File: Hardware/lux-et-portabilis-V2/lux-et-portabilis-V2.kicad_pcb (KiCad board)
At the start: 2 copper layers, 63 x 43 mm, 45 parts, among them J1 Conn_01x03_Socket, J2 Conn_01x03_Socket, J3 Conn_01x04_Socket, Q1 2N7002K, Q2 2N7002K, Q3 PMOS, U1 ESP32-C3-Supermini, U2 TP4056

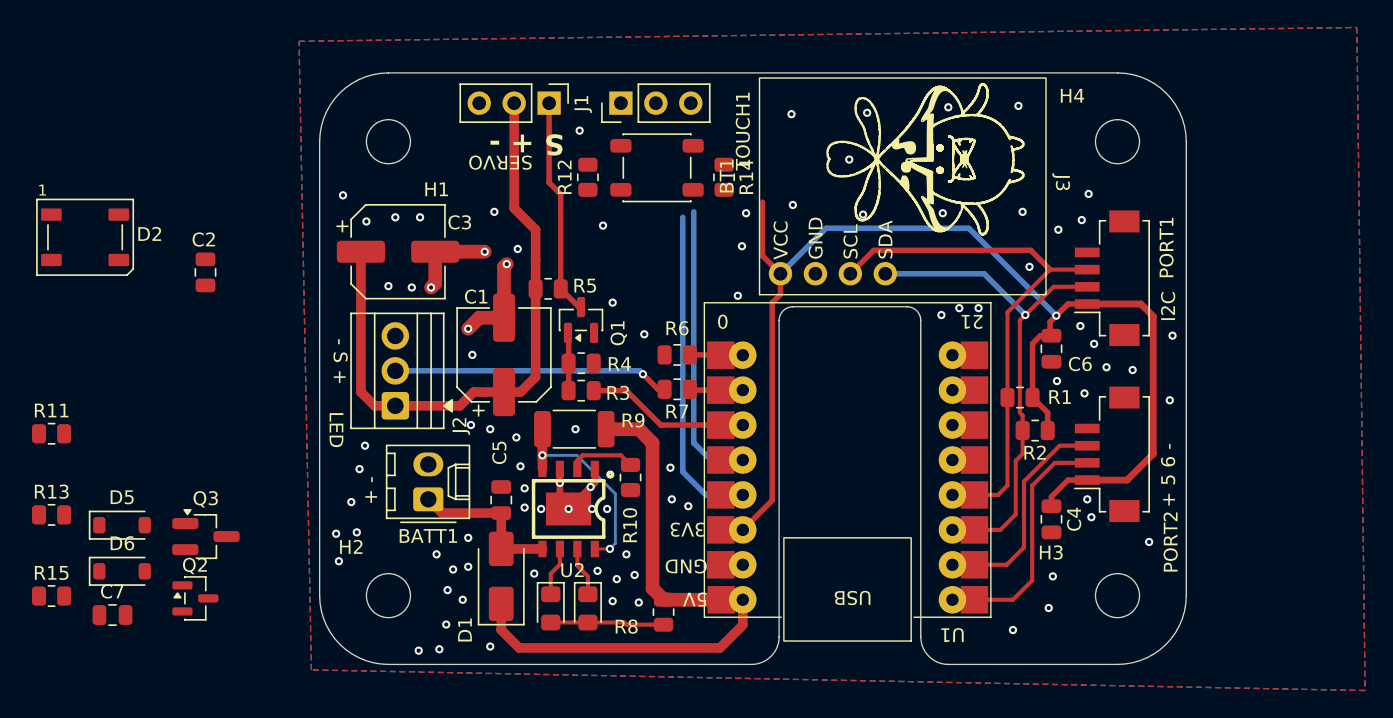
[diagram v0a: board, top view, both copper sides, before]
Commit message: Boot switch added, with connector for touch sensor
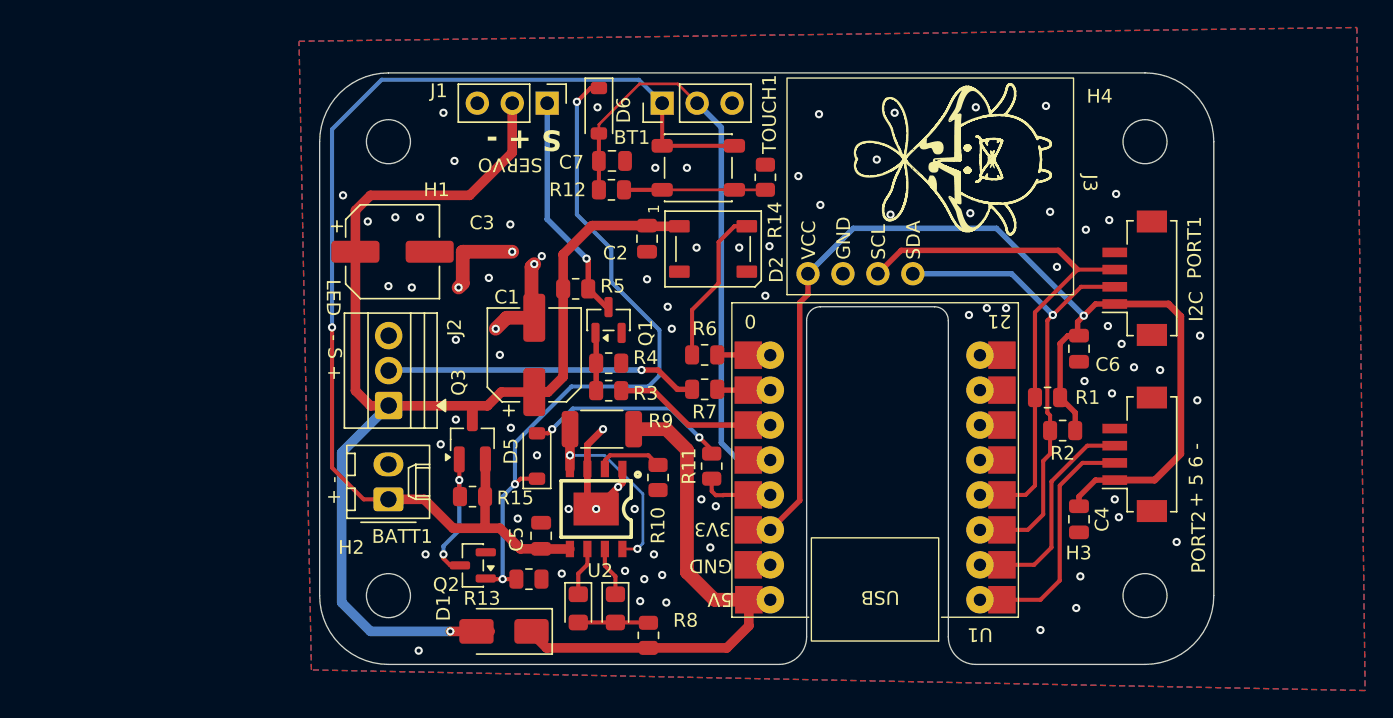
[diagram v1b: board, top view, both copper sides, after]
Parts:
- moved C7 49.1 mm to (130.8, 81.5), turned to 180 degrees
- moved D6 48.2 mm to (129.8, 77.8), turned to -90 degrees
- moved R11 48.0 mm to (138.0, 103.7), turned to 90 degrees
- moved D2 45.7 mm to (138.1, 87.9)
- moved R13 35.0 mm to (124.7, 111.9)
- moved C2 32.2 mm to (133.3, 87.2)
- moved R15 31.4 mm to (120.6, 105.9)
- moved D5 30.6 mm to (125.3, 103.0), turned to 90 degrees
- moved Q3 20.6 mm to (120.6, 101.7), turned to 90 degrees
- moved Q2 20.3 mm to (120.6, 110.9), turned to 180 degrees
- moved D1 4.00 mm to (122.9, 115.7), turned to 180 degrees
- moved C5 3.89 mm to (125.6, 108.8)
- moved BT1 3.00 mm to (137.0, 82.0)
- moved R14 3.00 mm to (141.9, 82.7)
- moved TOUCH1 3.00 mm to (134.4, 77.3)
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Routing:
- net +BATT: track 11.3 -> 83.8 mm, vias 0 -> 1
- net Net-(D5-K): track 0.00 -> 51.2 mm, vias 0 -> 3
- net V_REG: track 44.7 -> 91.9 mm, vias 0 -> 1
- net Button_GPIO: track 20.9 -> 43.2 mm
- net latch_enable: track 23.6 -> 3.69 mm
- net Net-(D5-A): track 0.00 -> 15.0 mm, vias 0 -> 2
- net Net-(D2-DIN): track 0.00 -> 11.5 mm
- net Net-(Q2-D): track 0.00 -> 10.3 mm, vias 0 -> 2
- net Net-(BT1-Pad2): track 0.00 -> 10.3 mm
- net +3.3V: track 86.7 -> 81.0 mm
- net +5V: track 42.2 -> 37.6 mm
- net GND: track 20.1 -> 23.5 mm, vias 89 -> 80
- net Net-(D3-A): track 8.27 -> 5.11 mm
- net Net-(J2-Pin_2): track 20.1 -> 22.2 mm
- net Net-(J1-Pin_1): track 15.9 -> 16.8 mm, vias 0 -> 1
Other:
- board size 63 x 43 mm -> 65 x 43 mm

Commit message: Fabrication files for Lux et Portabilis V2
Added power saving by shutting down the battery
Added onboard boot button
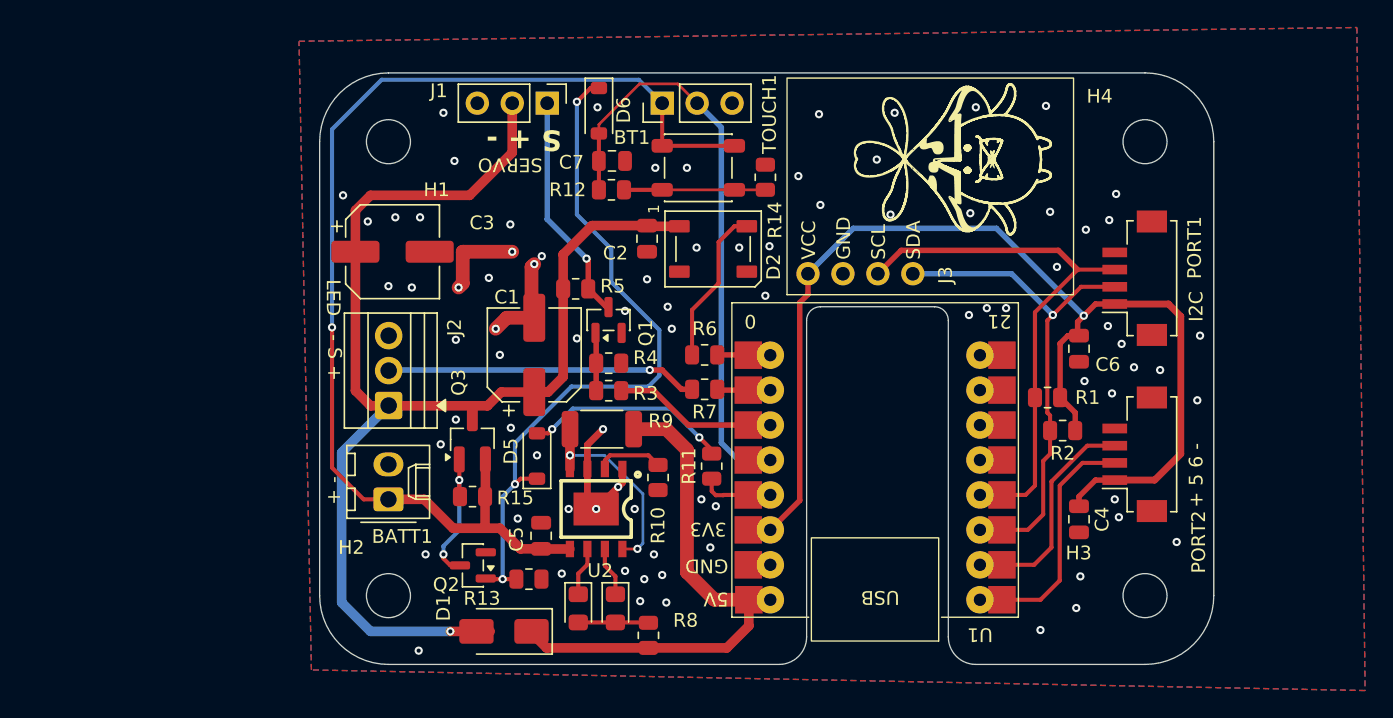
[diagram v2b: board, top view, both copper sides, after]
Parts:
- J3: footprint Custom_Footprints:MPU6050 -> Aleoexpress:MPU6050
- R1, R12, R2: value 2k2 -> 2.2k
- U1: footprint Custom_Footprints:ESP32-C3-Supermini -> Aleoexpress:ESP32-C3-Supermini
- U2: footprint Custom_Footprints:ESOP-8_L4.9-W3.9-P1.27-LS6.0-BL-EP -> Aleoexpress:ESOP-8_L4.9-W3.9-P1.27-LS6.0-BL-EP
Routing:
- net GND: vias 80 -> 82
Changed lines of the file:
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@@
 			)
 		)
-		(property "LCSC" "C77075"
+		(property "LCSC" "C15850"
 			(at 0 0 270)
 			(unlocked yes)
@@
 			)
 		)
-		(property "LCSC" "1"
+		(property "LCSC" "C7433470"
 			(at 0 0 90)
 			(unlocked yes)
@@
 		)
 	)
-	(footprint "Custom_Footprints:ESOP-8_L4.9-W3.9-P1.27-LS6.0-BL-EP"
+	(footprint "Aleoexpress:ESOP-8_L4.9-W3.9-P1.27-LS6.0-BL-EP"
 		(layer "F.Cu")
 		(at 129.6 106.8 180)
 		(property "Reference" "U2"
-			(at -0.28825 -4.4835 0)
+			(at -0.28825 -4.4835 180)
 			(layer "F.SilkS")
 			(effects
@@
 		)
 		(property "Value" "TP4056"
-			(at -0.28825 4.4835 0)
+			(at -0.28825 4.4835 180)
 			(layer "F.Fab")
 			(effects
@@
 		)
 		(property "Datasheet" "https://lcsc.com/datasheet/lcsc_datasheet_2410121619_TOPPOWER-Nanjing-Extension-Microelectronics-TP4056-42-ESOP8_C16581.pdf"
-			(at 0 0 0)
+			(at 0 0 180)
 			(layer "F.Fab")
 			(hide yes)
@@
 		)
 		(property "Description" "The Chip Type:Linear charging chip Supply Voltage:4V~6V Supply Voltage:4V~6V Maximum Charge Current:1A Charging Saturation Voltage:4.2V Type of Battery:Lithium-ion/Polymer Number of Cells:1 Number of Cells:1 Operating Temperature:-40°C~+85°C Operating Tempe"
-			(at 0 0 0)
-			(layer "F.Fab")
-			(hide yes)
-			(effects
-				(font
-					(size 1 1)
-					(thickness 0.15)
-				)
-			)
-		)
-		(property "Manufacturer Part" "TP4056"
 			(at 0 0 180)
-			(unlocked yes)
 			(layer "F.Fab")
 			(hide yes)
@@
 		)
 		(fp_text user "${REFERENCE}"
-			(at 0 0 0)
+			(at 0 0 180)
 			(layer "F.Fab")
 			(effects
@@
 			)
 		)
-		(property "LCSC" "1"
+		(property "LCSC" "C7433470"
 			(at 0 0 90)
 			(unlocked yes)
@@
 		(tags "LED RGB NeoPixel PLCC-4 5050")
 		(property "Reference" "D2"
-			(at 4.6 1.5 90)
+			(at 4.4 1.3 90)
 			(layer "F.SilkS")
 			(effects
@@
 			)
 		)
-		(property "LCSC" "C2162971"
+		(property "LCSC" "C25170691"
 			(at 0 0 90)
 			(unlocked yes)
@@
 			)
 		)
-		(property "Value" "2k2"
+		(property "Value" "2.2k"
 			(at 0 1.65 0)
 			(layer "F.Fab")
@@
 		)
 	)
-	(footprint "Custom_Footprints:ESP32-C3-Supermini"
+	(footprint "Aleoexpress:ESP32-C3-Supermini"
 		(layer "F.Cu")
 		(at 157.5 113.4 180)
@@
 		)
 		(fp_text user "GND"
-			(at 18 3.048 180)
+			(at 18.288 3.048 180)
 			(unlocked yes)
 			(layer "F.SilkS")
@@
 		)
 		(fp_text user "5V"
-			(at 18 0.6 180)
+			(at 18.288 0.635 180)
 			(unlocked yes)
 			(layer "F.SilkS")
@@
 		)
 		(fp_text user "3V3"
-			(at 18.1 5.715 180)
+			(at 18.415 5.715 180)
 			(unlocked yes)
 			(layer "F.SilkS")
@@
 			)
 		)
-		(property "LCSC" "C60491"
+		(property "LCSC" "C149504"
 			(at 0 0 270)
 			(unlocked yes)
@@
 			)
 		)
-		(property "Value" "2k2"
+		(property "Value" "2.2k"
 			(at 0 1.65 0)
 			(layer "F.Fab")
@@
 		)
 	)
-	(footprint "Custom_Footprints:MPU6050"
+	(footprint "Aleoexpress:MPU6050"
 		(layer "F.Cu")
 		(at 145 89.7 90)
 		(property "Reference" "J3"
-			(at 6.6 20.5 270)
+			(at -0.1 10 90)
 			(unlocked yes)
 			(layer "F.SilkS")
@@
 			)
 		)
-		(property "Value" "2k2"
+		(property "Value" "2.2k"
 			(at 0 1.65 0)
 			(layer "F.Fab")
@@
 			)
 		)
-		(property "LCSC" "C2162971"
+		(property "LCSC" "C25170691"
 			(at 0 0 0)
 			(unlocked yes)
@@
 			)
 		)
-		(property "LCSC" "C77075"
+		(property "LCSC" "C15850"
 			(at 0 0 270)
 			(unlocked yes)
@@
 			)
 		)
-		(property "LCSC" "C60491"
+		(property "LCSC" "C149504"
 			(at 0 0 0)
 			(unlocked yes)
@@
 			)
 		)
-		(property "LCSC" "C380331"
+		(property "LCSC" "C15850"
 			(at 0 0 90)
 			(unlocked yes)
@@
 	)
 	(via
+		(at 128.2 94.4)
+		(size 0.6)
+		(drill 0.3)
+		(layers "F.Cu" "B.Cu")
+		(free yes)
+		(net 1)
+	)
+	(via
 		(at 162.6 85.2)
 		(size 0.6)
@@
 	)
 	(via
+		(at 131.7 92.4)
+		(size 0.6)
+		(drill 0.3)
+		(layers "F.Cu" "B.Cu")
+		(free yes)
+		(net 1)
+	)
+	(via
 		(at 137.25 106.1)
 		(size 0.6)
@@
 	)
 	(segment
-		(start 136.575 98.1)
-		(end 135.5 98.1)
+		(start 135.8 98.1)
+		(end 134.4 96.7)
 		(width 0.4)
 		(layer "F.Cu")
@@
 	)
 	(segment
-		(start 135.5 98.1)
-		(end 134.1 96.7)
+		(start 136.575 98.1)
+		(end 135.8 98.1)
 		(width 0.4)
 		(layer "F.Cu")
@@
 	)
 	(segment
-		(start 134.1 96.7)
-		(end 132.9 96.7)
+		(start 134.4 96.7)
+		(end 133.5 96.7)
 		(width 0.4)
 		(layer "F.Cu")
@@
 	)
 	(via
-		(at 132.9 96.7)
+		(at 133.5 96.7)
 		(size 0.6)
 		(drill 0.3)
@@
 	)
 	(segment
-		(start 115.06 96.7)
-		(end 132.9 96.7)
+		(start 115 96.76)
+		(end 115.06 96.7)
 		(width 0.4)
 		(layer "B.Cu")
@@
 	)
 	(segment
-		(start 115 96.76)
-		(end 115.06 96.7)
+		(start 115.06 96.7)
+		(end 133.5 96.7)
 		(width 0.4)
 		(layer "B.Cu")

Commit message: Added ADC reading to Portabilis V2
Plus board render
Changed Status LED pin to GPIO10
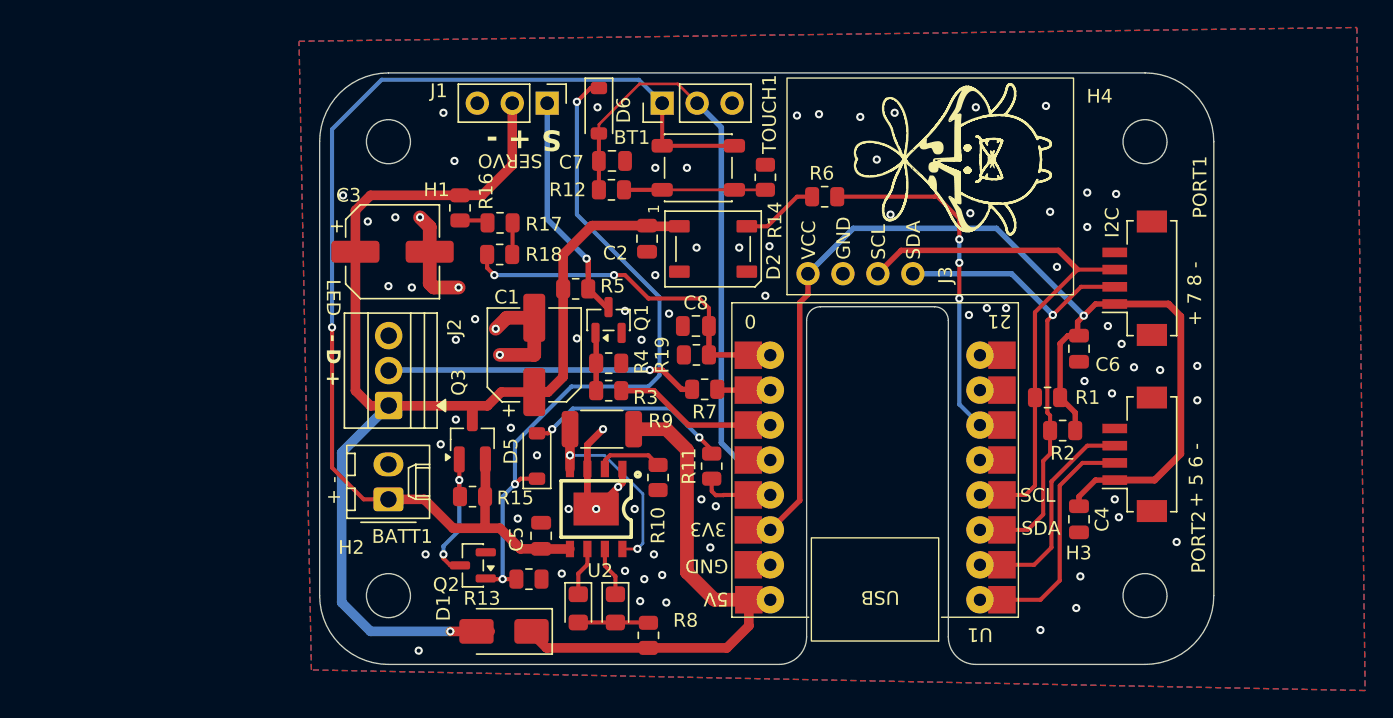
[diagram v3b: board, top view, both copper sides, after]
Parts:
- added C8: 100nF, Capacitor_SMD:C_0805_2012Metric, F.Cu at (136.8, 93.5)
- added R16: 100k, Resistor_SMD:R_0805_2012Metric, F.Cu at (119.7, 84.9)
- added R17: 100k, Resistor_SMD:R_0805_2012Metric, F.Cu at (122.6, 86.0)
- added R18: 100k, Resistor_SMD:R_0805_2012Metric, F.Cu at (122.6, 88.3)
- added R19: 100k, Resistor_SMD:R_0805_2012Metric, F.Cu at (136.9, 95.6)
- moved R6 14.4 mm to (146.2, 84.1)
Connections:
- net Button renamed OB_Button
- U1 pad 6: unconnected-(U1-GPIO10-Pad6) -> Status_LED
- U1 pad 9: Status_LED -> ADC1_0
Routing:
- net ADC1_0: track 0.00 -> 26.2 mm, vias 0 -> 2
- net Status_LED: track 2.27 -> 25.2 mm, vias 0 -> 3
- net Net-(D2-DIN): track 11.5 -> 5.64 mm
- net GND: track 23.5 -> 25.9 mm, vias 82 -> 78
- net Net-(R17-Pad1): track 0.00 -> 2.31 mm
- net Net-(R16-Pad1): track 0.00 -> 2.07 mm
- net V_REG: track 91.9 -> 92.4 mm
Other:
- board text added: "+ 7 8 -"
- board text added: "- D +"
- board text added: "SCL"
- board text added: "SDA"
- board text removed: "- S +"

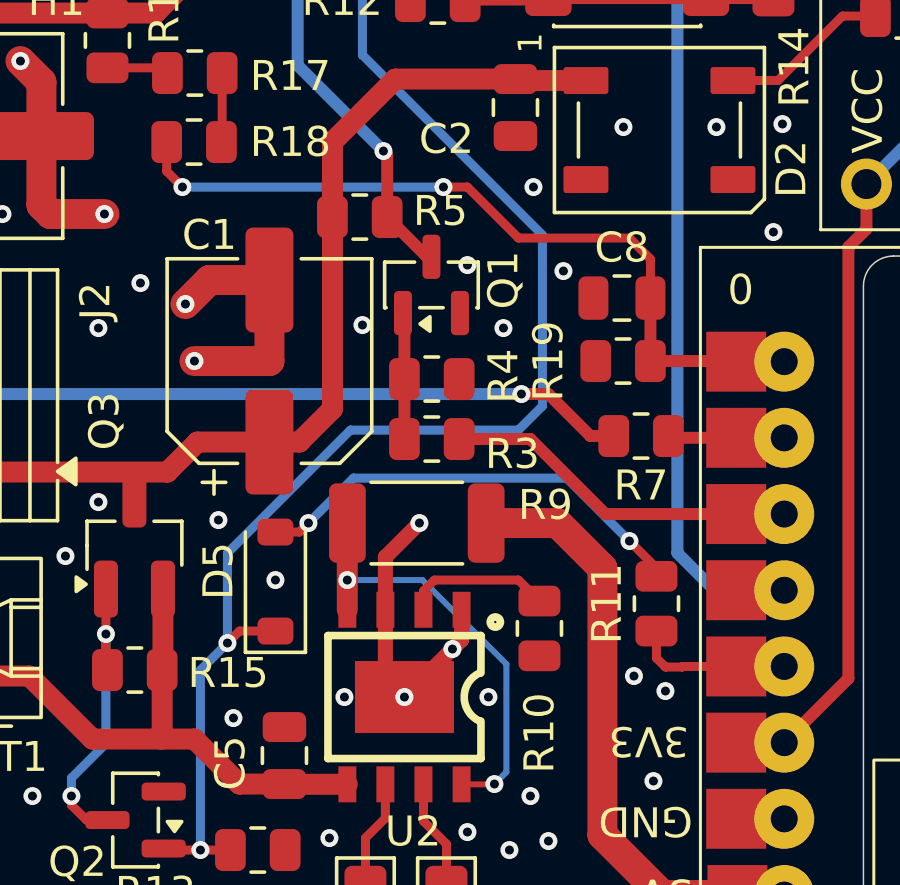
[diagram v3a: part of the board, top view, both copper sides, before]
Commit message: Added Marajoara V2 - ESP32 + I2S Audio
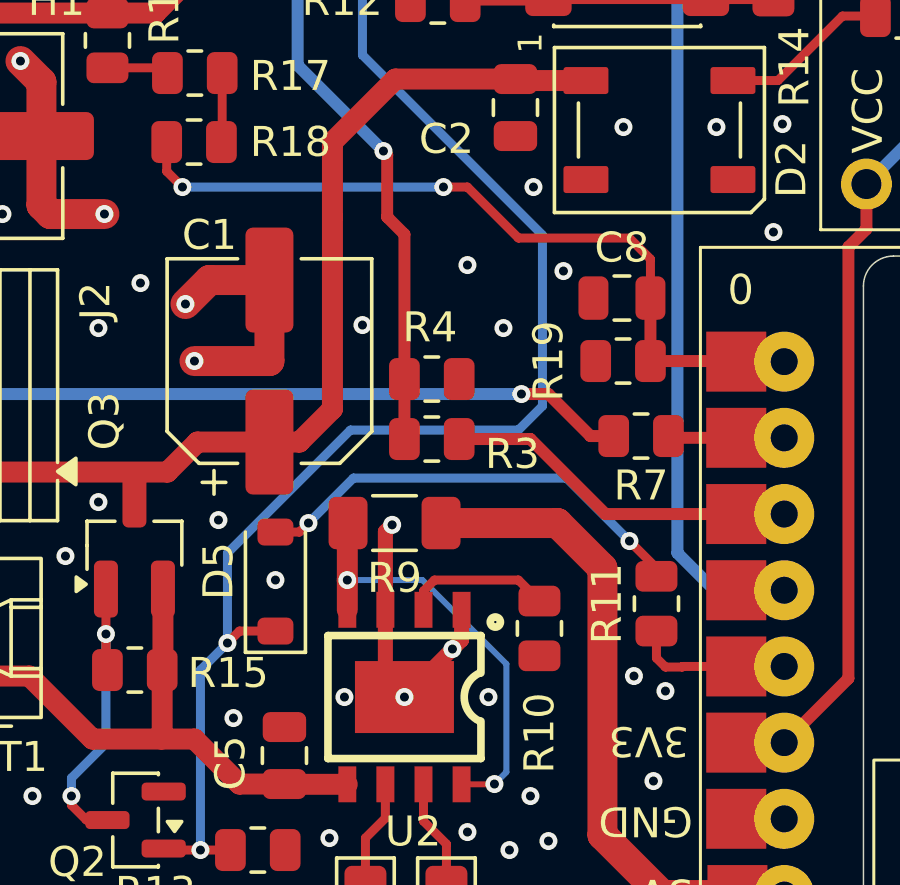
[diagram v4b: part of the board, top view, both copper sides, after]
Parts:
- removed Q1: 2N7002K, Package_TO_SOT_SMD:SOT-23
- removed R5: 10k, Resistor_SMD:R_0805_2012Metric
- R9: footprint Resistor_SMD:R_2010_5025Metric -> Resistor_SMD:R_1206_3216Metric_Pad1.30x1.75mm_HandSolder
- moved R9 0.74 mm to (129.3, 101.0)
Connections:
- R3 pad 2: Net-(Q1-G) -> Net-(J1-Pin_1)
- R4 pad 1: Net-(Q1-G) -> Net-(J1-Pin_1)
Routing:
- net Net-(J1-Pin_1): track 16.8 -> 22.4 mm
- net Net-(Q1-G): track 4.22 -> 0.00 mm
- net +5V: track 37.6 -> 39.1 mm
